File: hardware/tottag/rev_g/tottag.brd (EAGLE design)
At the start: 68.1 x 39.6 mm, 200 parts, among them J1 USB4110-GF-A, J2 DM3AT-SF-PEJM5, J3 TC2030-JLINK-NL-2SIDE, J4 TC2030-JLINK-NL-2SIDE, J5 MOLEX-PICO-SPOX-3SIDE, Q1 CSD75207W15, Q4 CSD75207W15, T1 HHM1595A1, U1 DW1000, U10 STM32F091CC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

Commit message: rev_g: small trace fixes; plane cleanups
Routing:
- net GND: vias 538 -> 539
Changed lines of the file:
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@@
 <via x="-13.1064" y="10.16" extent="1-16" drill="0.2032"/>
 <via x="-2.032" y="0.508" extent="1-16" drill="0.2032"/>
-<via x="-12.5222" y="19.7104" extent="1-16" drill="0.2032"/>
+<via x="-13.0302" y="20.2184" extent="1-16" drill="0.2032"/>
 <via x="-15.9258" y="20.447" extent="1-16" drill="0.2032"/>
 <via x="-7.5692" y="20.5232" extent="1-16" drill="0.2032"/>
 <via x="-10.8204" y="20.4724" extent="1-16" drill="0.2032"/>
-<via x="-12.4968" y="20.3708" extent="1-16" drill="0.2032"/>
+<via x="-12.4968" y="20.574" extent="1-16" drill="0.2032"/>
 <via x="-14.097" y="9.0932" extent="1-16" drill="0.2032"/>
 <via x="19.2532" y="17.9832" extent="1-16" drill="0.2032"/>
@@
 <vertex x="-3.8608" y="21.6408"/>
 <vertex x="-13.9192" y="21.6408"/>
-<vertex x="-13.9192" y="20.5232"/>
-<vertex x="-3.8608" y="20.5232"/>
+<vertex x="-13.9192" y="20.7264"/>
+<vertex x="-3.8608" y="20.7264"/>
 </polygon>
 <polygon width="0.1016" layer="16" rank="6">
@@
 <vertex x="-3.6576" y="21.6408"/>
 <vertex x="-13.9192" y="21.6408"/>
-<vertex x="-13.9192" y="20.5232"/>
-<vertex x="-3.6576" y="20.5232"/>
+<vertex x="-13.9192" y="20.7264"/>
+<vertex x="-3.6576" y="20.7264"/>
 </polygon>
 <polygon width="0.1016" layer="16" rank="6">
@@
 <vertex x="-25.1968" y="17.78"/>
 </polygon>
+<via x="-13.5382" y="19.7104" extent="1-16" drill="0.2032"/>
 </signal>
 <signal name="VUSB">
@@
 <wire x1="21.48966875" y1="18.0848" x2="21.1328" y2="18.0848" width="0.2032" layer="1"/>
 <via x="21.1328" y="18.0848" extent="1-16" drill="0.2032"/>
-<wire x1="21.1328" y1="18.0848" x2="21.336" y2="18.0848" width="0.2032" layer="15"/>
-<wire x1="21.336" y1="18.0848" x2="22.1234" y2="17.2974" width="0.2032" layer="15"/>
-<wire x1="22.1234" y1="17.2974" x2="24.765" y2="17.2974" width="0.2032" layer="15"/>
+<wire x1="21.1328" y1="18.0848" x2="21.7424" y2="18.0848" width="0.2032" layer="15"/>
+<wire x1="21.7424" y1="18.0848" x2="22.5298" y2="17.2974" width="0.2032" layer="15"/>
+<wire x1="22.5298" y1="17.2974" x2="24.765" y2="17.2974" width="0.2032" layer="15"/>
 <wire x1="24.765" y1="17.2974" x2="25.1968" y2="16.8656" width="0.2032" layer="15"/>
 <wire x1="24.384" y1="9.7536" x2="25.5016" y2="8.636" width="0.2032" layer="15"/>
@@
 <wire x1="20.21966875" y1="17.9832" x2="19.9136" y2="17.9832" width="0.2032" layer="1"/>
 <via x="19.9136" y="17.9832" extent="1-16" drill="0.2032"/>
-<wire x1="19.9136" y1="17.9832" x2="20.6248" y2="17.9832" width="0.2032" layer="15"/>
-<wire x1="20.6248" y1="17.9832" x2="21.6154" y2="16.9926" width="0.2032" layer="15"/>
-<wire x1="24.5618" y1="16.9926" x2="24.892" y2="16.6624" width="0.2032" layer="15"/>
-<wire x1="21.6154" y1="16.9926" x2="24.5618" y2="16.9926" width="0.2032" layer="15"/>
+<wire x1="24.892" y1="16.6624" x2="24.5618" y2="16.9926" width="0.2032" layer="15"/>
 <wire x1="24.0792" y1="10.6157125" x2="24.0792" y2="9.62734375" width="0.2032" layer="15"/>
 <wire x1="24.892" y1="16.6624" x2="24.892" y2="11.4285125" width="0.2032" layer="15"/>
@@
 <wire x1="28.9052" y1="-1.524" x2="28.9306" y2="-1.5494" width="0.2032" layer="16"/>
 <wire x1="29.8704" y1="3.57575625" x2="29.8704" y2="1.4891375" width="0.2032" layer="15"/>
+<wire x1="20.9644625" y1="17.6784" x2="20.6596625" y2="17.9832" width="0.2032" layer="15"/>
+<wire x1="21.71774375" y1="17.6784" x2="20.9644625" y2="17.6784" width="0.2032" layer="15"/>
+<wire x1="24.5618" y1="16.9926" x2="22.40354375" y2="16.9926" width="0.2032" layer="15"/>
+<wire x1="22.40354375" y1="16.9926" x2="21.71774375" y2="17.6784" width="0.2032" layer="15"/>
+<wire x1="20.6596625" y1="17.9832" x2="19.9136" y2="17.9832" width="0.2032" layer="15"/>
 </signal>
 <signal name="NRF_DECAP1">
@@
 <wire x1="-9.7536" y1="11.684" x2="-10.5664" y2="10.8712" width="0.2032" layer="16"/>
 <via x="-10.5664" y="10.8712" extent="1-16" drill="0.2032"/>
-<wire x1="-21.2344" y1="10.4648" x2="-22.1488" y2="11.3792" width="0.2032" layer="15"/>
 <via x="-22.1488" y="11.3792" extent="1-16" drill="0.2032"/>
 <wire x1="-10.5664" y1="10.8712" x2="-10.7696" y2="10.668" width="0.2032" layer="15"/>
-<wire x1="-10.7696" y1="10.668" x2="-19.5072" y2="10.668" width="0.2032" layer="15"/>
-<wire x1="-19.5072" y1="10.668" x2="-19.7104" y2="10.4648" width="0.2032" layer="15"/>
-<wire x1="-19.7104" y1="10.4648" x2="-21.2344" y2="10.4648" width="0.2032" layer="15"/>
+<wire x1="-19.5072" y1="10.668" x2="-10.7696" y2="10.668" width="0.2032" layer="15"/>
 <wire x1="-21.3337" y1="11.0402" x2="-21.8098" y2="11.0402" width="0.2032" layer="1"/>
 <wire x1="-21.8098" y1="11.0402" x2="-22.1488" y2="11.3792" width="0.2032" layer="1"/>
+<wire x1="-22.1488" y1="11.3792" x2="-20.2184" y2="11.3792" width="0.2032" layer="15"/>
+<wire x1="-20.2184" y1="11.3792" x2="-19.5072" y2="10.668" width="0.2032" layer="15"/>
 </signal>
 <signal name="+1V8">

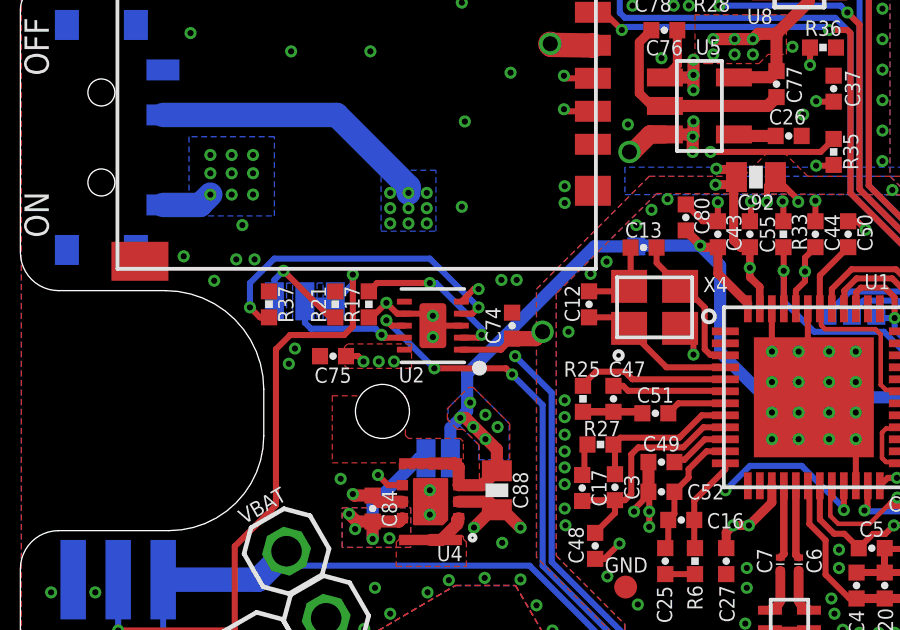
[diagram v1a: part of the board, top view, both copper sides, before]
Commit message: rev_g: return N$34 to layer 15
here layer 16 plane is more valuable
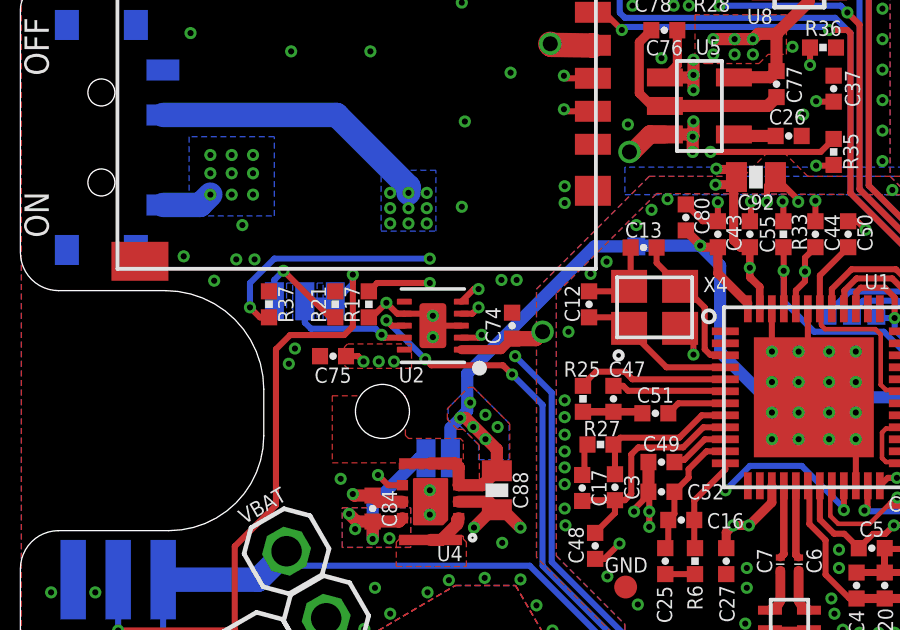
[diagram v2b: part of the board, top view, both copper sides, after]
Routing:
- net N$49: vias 2 -> 3
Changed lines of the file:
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@@
 <wire x1="-18.7896" y1="15.9576" x2="-18.6944" y2="16.0528" width="0.2032" layer="1"/>
 <via x="-18.6944" y="16.0528" extent="1-16" drill="0.2032"/>
-<wire x1="-18.6944" y1="16.0528" x2="-18.6944" y2="16.256" width="0.2032" layer="16"/>
-<wire x1="-18.6944" y1="16.256" x2="-20.2184" y2="17.78" width="0.2032" layer="16"/>
-<wire x1="-20.2184" y1="17.78" x2="-20.4216" y2="17.78" width="0.2032" layer="16"/>
+<wire x1="-18.6944" y1="16.0528" x2="-18.6944" y2="16.256" width="0.2032" layer="15"/>
+<wire x1="-18.6944" y1="16.256" x2="-20.2184" y2="17.78" width="0.2032" layer="15"/>
+<wire x1="-20.2184" y1="17.78" x2="-20.4216" y2="17.78" width="0.2032" layer="15"/>
 <via x="-20.4216" y="17.78" extent="1-16" drill="0.2032"/>
 <wire x1="-20.4216" y1="17.78" x2="-22.17546875" y2="17.78" width="0.2032" layer="1"/>
@@
 <wire x1="-19.0056" y1="16.7576" x2="-18.796" y2="16.9672" width="0.2032" layer="1"/>
 <via x="-18.796" y="16.9672" extent="1-16" drill="0.2032"/>
-<wire x1="-18.796" y1="16.9672" x2="-20.4216" y2="18.5928" width="0.2032" layer="16"/>
+<wire x1="-18.796" y1="16.9672" x2="-20.4216" y2="18.5928" width="0.2032" layer="15"/>
 <wire x1="-25.6032" y1="18.5928" x2="-26.416" y2="17.78" width="0.2032" layer="16"/>
 <wire x1="-26.416" y1="16.9672" x2="-26.416" y2="17.78" width="0.2032" layer="16"/>
@@
 <wire x1="-26.0858" y1="16.63573125" x2="-26.416634375" y2="16.966565625" width="0.2032" layer="1"/>
 <wire x1="-26.416" y1="16.9672" x2="-26.416634375" y2="16.966565625" width="0.2032" layer="1"/>
+<via x="-20.4216" y="18.5928" extent="1-16" drill="0.2032"/>
 </signal>
 <signal name="!CHG">
@@
 <wire x1="-16.6624" y1="13.716" x2="-17.6784" y2="14.732" width="0.2032" layer="16"/>
 <via x="-17.6784" y="14.732" extent="1-16" drill="0.2032"/>
-<wire x1="-17.6784" y1="14.732" x2="-17.8816" y2="14.9352" width="0.2032" layer="1"/>
-<wire x1="-17.8816" y1="14.9352" x2="-20.2692" y2="14.9352" width="0.2032" layer="1"/>
-<wire x1="-20.2692" y1="14.9352" x2="-21.8694" y2="16.5354" width="0.2032" layer="16"/>
-<via x="-20.2692" y="14.9352" extent="1-16" drill="0.2032"/>
+<wire x1="-17.6784" y1="14.732" x2="-17.9832" y2="15.0368" width="0.2032" layer="1"/>
+<wire x1="-17.9832" y1="15.0368" x2="-20.3708" y2="15.0368" width="0.2032" layer="1"/>
+<wire x1="-20.3708" y1="15.0368" x2="-20.574" y2="15.24" width="0.2032" layer="1"/>
+<wire x1="-20.574" y1="15.24" x2="-21.8694" y2="16.5354" width="0.2032" layer="16"/>
+<via x="-20.574" y="15.24" extent="1-16" drill="0.2032"/>
 </signal>
 <signal name="!PG">
@@
 </polygon>
 <contactref element="C74" pad="1"/>
-<wire x1="-17.6784" y1="15.92453125" x2="-18.04533125" y2="15.5576" width="0.2032" layer="1"/>
-<wire x1="-18.04533125" y1="15.5576" x2="-19.37" y2="15.5576" width="0.2032" layer="1"/>
+<wire x1="-17.6784" y1="15.92453125" x2="-18.04533125" y2="15.5576" width="0.3048" layer="1"/>
+<wire x1="-18.04533125" y1="15.5576" x2="-19.37" y2="15.5576" width="0.3048" layer="1"/>
 <wire x1="-17.6784" y1="15.92453125" x2="-16.89226875" y2="15.92453125" width="0.508" layer="1"/>
 <wire x1="-16.89226875" y1="15.92453125" x2="-16.6624" y2="16.1544" width="0.508" layer="1"/>

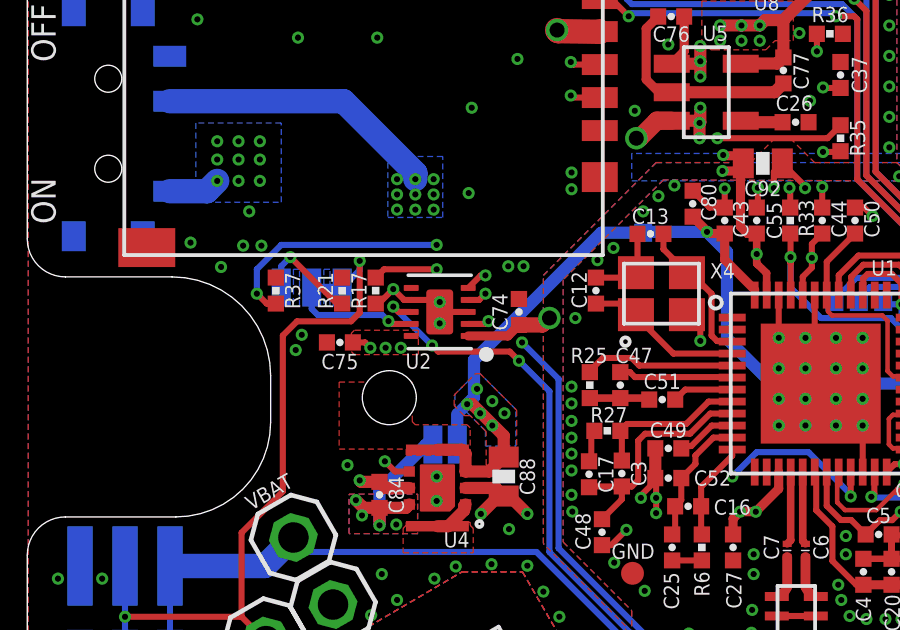
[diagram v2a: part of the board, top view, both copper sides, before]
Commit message: rev_g: finish messing with planes on left side
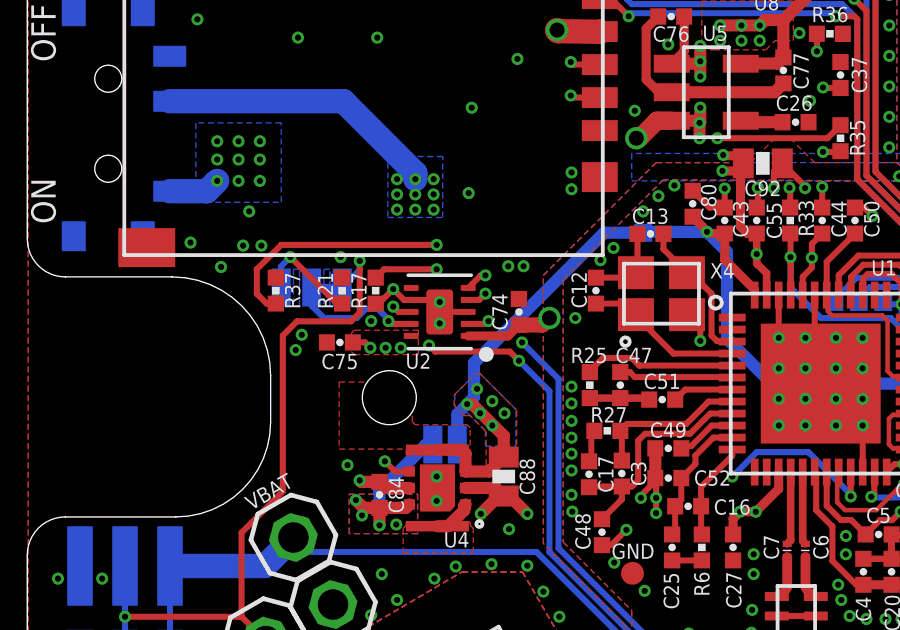
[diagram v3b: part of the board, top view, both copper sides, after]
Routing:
- net N$49: vias 3 -> 2
- net GND: vias 539 -> 541
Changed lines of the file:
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@@
 <via x="14.732" y="3.6322" extent="1-16" drill="0.2032"/>
 <via x="-15.9258" y="21.0058" extent="1-16" drill="0.2032"/>
-<via x="-15.0622" y="18.0848" extent="1-16" drill="0.2032"/>
+<via x="-14.9606" y="18.0848" extent="1-16" drill="0.2032"/>
 <via x="-18.9484" y="9.6266" extent="1-16" drill="0.2032"/>
 <via x="-15.9258" y="13.3096" extent="1-16" drill="0.2032"/>
@@
 </polygon>
 <via x="-13.5382" y="19.7104" extent="1-16" drill="0.2032"/>
+<via x="-22.606" y="16.0528" extent="1-16" drill="0.2032"/>
+<via x="-23.622" y="18.1864" extent="1-16" drill="0.2032"/>
 </signal>
 <signal name="VUSB">
@@
 <wire x1="-19.4587" y1="11.6355" x2="-19.4587" y2="11.0402" width="0.4064" layer="1"/>
 <wire x1="-19.5884" y1="11.7652" x2="-19.4587" y2="11.6355" width="0.4064" layer="1"/>
-<wire x1="-19.177" y1="14.7574" x2="-19.177" y2="13.5128" width="0.4064" layer="16"/>
+<wire x1="-19.177" y1="14.6558" x2="-19.177" y2="13.5128" width="0.4064" layer="16"/>
 <via x="-18.161" y="12.9794" extent="1-16" drill="0.2032"/>
 <via x="-19.0754" y="13.7922" extent="1-16" drill="0.2032"/>
@@
 <via x="-18.9738" y="12.9794" extent="1-16" drill="0.2032"/>
 <via x="-18.5674" y="13.3858" extent="1-16" drill="0.2032"/>
-<wire x1="-13.5382" y1="18.9992" x2="-14.9352" y2="18.9992" width="0.4064" layer="16"/>
-<wire x1="-14.9352" y1="18.9992" x2="-19.177" y2="14.7574" width="0.4064" layer="16"/>
+<wire x1="-13.5382" y1="18.9992" x2="-14.8336" y2="18.9992" width="0.4064" layer="16"/>
+<wire x1="-14.8336" y1="18.9992" x2="-19.177" y2="14.6558" width="0.4064" layer="16"/>
 <wire x1="-11.40968125" y1="19.026515625" x2="-10.7442" y2="18.361034375" width="0.4064" layer="16"/>
 <wire x1="-10.7442" y1="18.361034375" x2="-10.7442" y2="15.4686" width="0.4064" layer="16"/>
@@
 <wire x1="-21.933825" y1="15.9576" x2="-22.029025" y2="16.0528" width="0.2032" layer="1"/>
 <via x="-22.029025" y="16.0528" extent="1-16" drill="0.2032"/>
-<wire x1="-22.232225" y1="16.256" x2="-24.384" y2="16.256" width="0.2032" layer="16"/>
-<wire x1="-22.232225" y1="16.256" x2="-22.029025" y2="16.0528" width="0.2032" layer="16"/>
-<wire x1="-24.5872" y1="16.4592" x2="-24.384" y2="16.256" width="0.2032" layer="16"/>
-<wire x1="-24.5872" y1="17.1704" x2="-24.5872" y2="16.4592" width="0.2032" layer="16"/>
+<wire x1="-22.029025" y1="16.0528" x2="-22.029025" y2="16.1036" width="0.2032" layer="16"/>
+<wire x1="-22.029025" y1="16.1036" x2="-22.384625" y2="16.4592" width="0.2032" layer="16"/>
+<wire x1="-24.5872" y1="16.5608" x2="-24.5872" y2="17.1704" width="0.2032" layer="16"/>
+<wire x1="-22.384625" y1="16.4592" x2="-22.7838" y2="16.4592" width="0.2032" layer="16"/>
+<wire x1="-24.1808" y1="16.1544" x2="-24.5872" y2="16.5608" width="0.2032" layer="16"/>
+<wire x1="-22.7838" y1="16.4592" x2="-23.0886" y2="16.1544" width="0.2032" layer="16"/>
+<wire x1="-23.0886" y1="16.1544" x2="-24.1808" y2="16.1544" width="0.2032" layer="16"/>
 </signal>
 <signal name="N$47">
@@
 <via x="-18.796" y="16.9672" extent="1-16" drill="0.2032"/>
 <wire x1="-18.796" y1="16.9672" x2="-20.4216" y2="18.5928" width="0.2032" layer="15"/>
-<wire x1="-25.6032" y1="18.5928" x2="-26.416" y2="17.78" width="0.2032" layer="16"/>
-<wire x1="-26.416" y1="16.9672" x2="-26.416" y2="17.78" width="0.2032" layer="16"/>
-<via x="-26.416" y="16.9672" extent="1-16" drill="0.2032"/>
-<wire x1="-20.4216" y1="18.5928" x2="-25.6032" y2="18.5928" width="0.2032" layer="16"/>
+<wire x1="-25.6032" y1="18.5928" x2="-26.416" y2="17.78" width="0.2032" layer="1"/>
+<wire x1="-26.416" y1="16.9672" x2="-26.416" y2="17.78" width="0.2032" layer="1"/>
+<wire x1="-20.4216" y1="18.5928" x2="-25.6032" y2="18.5928" width="0.2032" layer="1"/>
 <wire x1="-25.781" y1="16.63573125" x2="-26.0858" y2="16.63573125" width="0.2032" layer="1"/>
 <wire x1="-26.0858" y1="16.63573125" x2="-26.416634375" y2="16.966565625" width="0.2032" layer="1"/>
@@
 <via x="-17.6784" y="14.732" extent="1-16" drill="0.2032"/>
 <wire x1="-17.6784" y1="14.732" x2="-17.9832" y2="15.0368" width="0.2032" layer="1"/>
-<wire x1="-17.9832" y1="15.0368" x2="-20.3708" y2="15.0368" width="0.2032" layer="1"/>
-<wire x1="-20.3708" y1="15.0368" x2="-20.574" y2="15.24" width="0.2032" layer="1"/>
-<wire x1="-20.574" y1="15.24" x2="-21.8694" y2="16.5354" width="0.2032" layer="16"/>
-<via x="-20.574" y="15.24" extent="1-16" drill="0.2032"/>
+<wire x1="-17.9832" y1="15.0368" x2="-20.4724" y2="15.0368" width="0.2032" layer="1"/>
+<wire x1="-20.4724" y1="15.0368" x2="-20.6756" y2="15.24" width="0.2032" layer="1"/>
+<wire x1="-20.6756" y1="15.24" x2="-20.6756" y2="15.3416" width="0.2032" layer="2"/>
+<wire x1="-20.6756" y1="15.3416" x2="-21.8694" y2="16.5354" width="0.2032" layer="2"/>
+<via x="-20.6756" y="15.24" extent="1-16" drill="0.2032"/>
 </signal>
 <signal name="!PG">

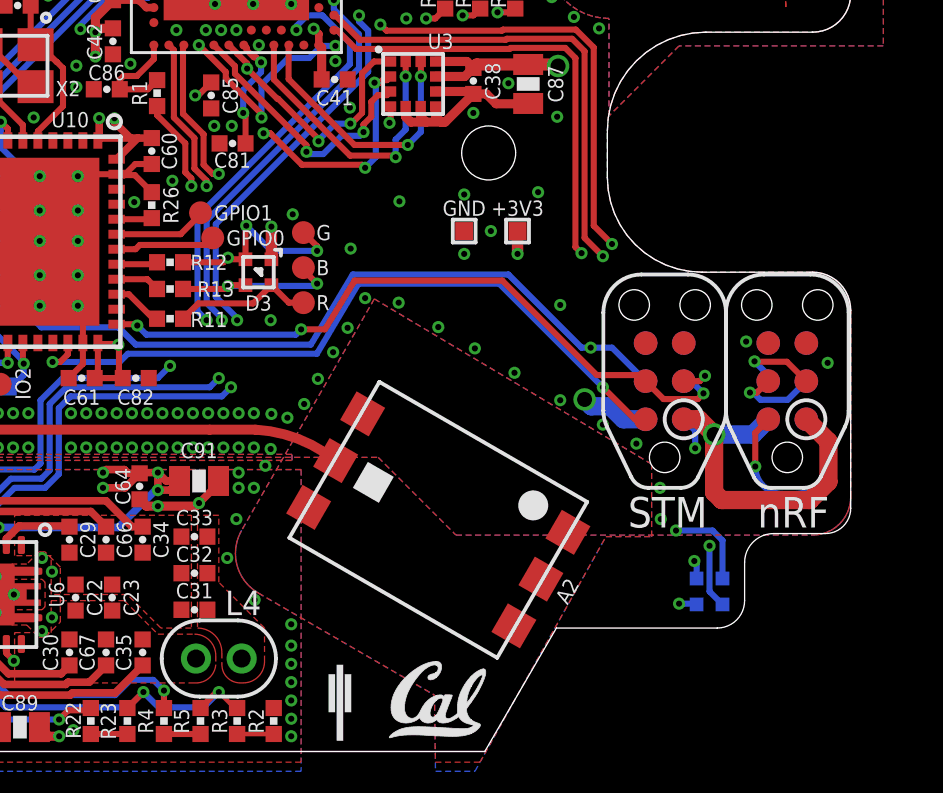
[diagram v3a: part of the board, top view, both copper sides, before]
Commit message: rev_g: move STM LED to light pipe too
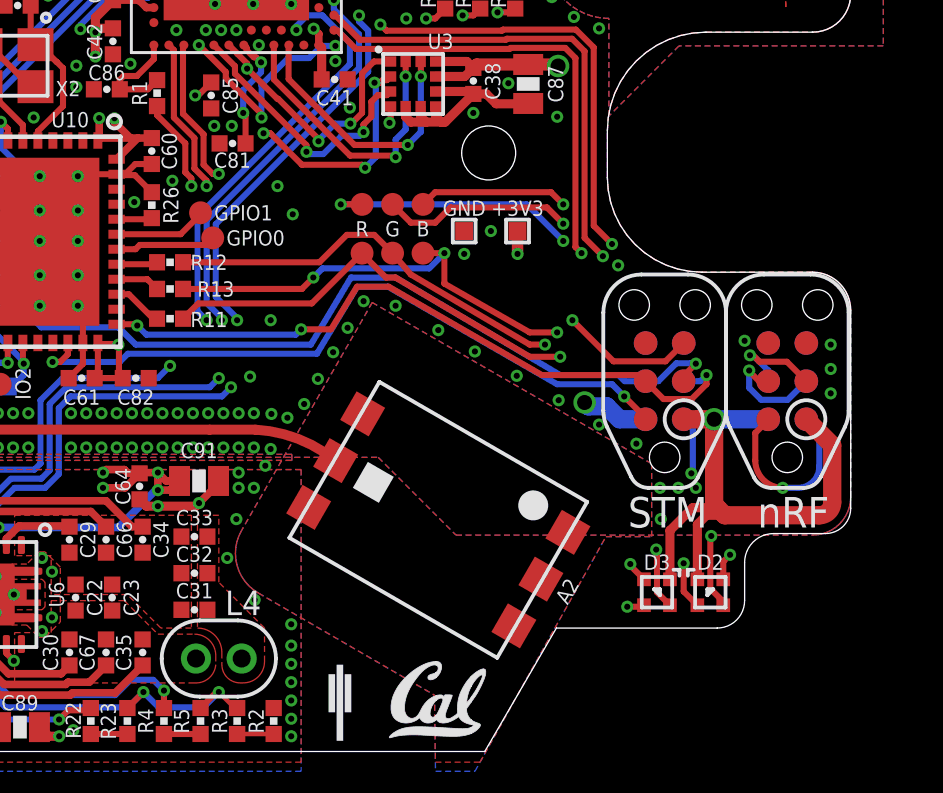
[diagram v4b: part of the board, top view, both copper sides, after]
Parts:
- added TP16, TP17, TP18: TEST-POINT, headers:PAD.03X.03
- moved D3 17.0 mm to (27.6, -1.14)
- moved TP9 4.02 mm to (19.8, 10.2)
- moved TP7 3.05 mm to (18.8, 10.2)
- moved TP8 2.56 mm to (17.8, 10.2)
- flipped D2 to the top
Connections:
- net N$59: now also TP16.P$1
- net N$60: now also TP17.P$1
- net N$61: now also TP18.P$1
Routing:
- net N$24: track 5.86 -> 32.1 mm, vias 2 -> 4
- net N$25: track 4.72 -> 29.2 mm, vias 0 -> 2
- net N$23: track 6.80 -> 29.0 mm, vias 3 -> 2
- net N$59: track 27.8 -> 36.2 mm, vias 2 -> 4
- net N$60: track 28.7 -> 36.2 mm, vias 2 -> 3
- net N$61: track 30.1 -> 34.7 mm, vias 2 -> 3
- net GND: track 169.0 -> 173.6 mm, vias 541 -> 544
- net +3V3: track 140.9 -> 144.5 mm, vias 43 -> 41
- net !STM_RST: track 36.3 -> 33.4 mm, vias 3 -> 2
- net NRF_SWDIO: track 32.3 -> 33.1 mm
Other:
- board text added: "Light Pipe Aperature (LEDs should be under this)"
